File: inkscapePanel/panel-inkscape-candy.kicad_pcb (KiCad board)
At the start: 2 copper layers, 99.9 x 38.9 mm, 39 parts

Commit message: new panel
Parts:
- removed the G*** at (0.00, 0.00) (x6)
- added G*** (x6): LOGO, LOGO, F.Cu at (0.00, 0.00)

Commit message: single
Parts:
- removed the G*** at (0.00, 0.00) (x6)
- added G*** (x6): LOGO, LOGO, F.Cu at (0.00, 0.00)

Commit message: sent to fab
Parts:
- removed the ? at (47.0, 28.6)
- removed the ? at (30.8, 34.3)
- removed the ? at (14.2, 28.6)
- removed the ? at (14.3, 29.6)
- removed the ? at (14.3, 30.5)
- removed the ? at (14.2, 31.4)
- removed the ? at (16.6, 28.7)
- removed the ? at (16.6, 29.6)
- removed the ? at (47.0, 29.6)
- removed the ? at (16.6, 30.5)
- removed the ? at (16.6, 31.4)
- removed the ? at (47.0, 30.5)
- removed the ? at (-46.7, 28.7)
- removed the ? at (-46.8, 29.7)
- removed the ? at (-46.8, 30.6)
- removed the ? at (-46.7, 31.5)
- removed the ? at (47.0, 31.4)
- removed the ? at (19.0, 28.6)
- removed the G*** at (0.00, 0.00) (x6)
- added ?: , Wire_Pads:SolderWirePad_single_0-8mmDrill, F.Cu at (44.8, 28.9)
- added ?: , Wire_Pads:SolderWirePad_single_0-8mmDrill, F.Cu at (30.7, 34.0)
- added ?: , Wire_Pads:SolderWirePad_single_0-8mmDrill, F.Cu at (14.3, 28.7)
- added ?: , Wire_Pads:SolderWirePad_single_0-8mmDrill, F.Cu at (14.4, 29.7)
- added ?: , Wire_Pads:SolderWirePad_single_0-8mmDrill, F.Cu at (14.4, 30.6)
- added ?: , Wire_Pads:SolderWirePad_single_0-8mmDrill, F.Cu at (14.4, 31.4)
- added ?: , Wire_Pads:SolderWirePad_single_0-8mmDrill, F.Cu at (16.5, 28.8)
- added ?: , Wire_Pads:SolderWirePad_single_0-8mmDrill, F.Cu at (16.4, 29.6)
- added ?: , Wire_Pads:SolderWirePad_single_0-8mmDrill, F.Cu at (45.0, 29.7)
- added ?: , Wire_Pads:SolderWirePad_single_0-8mmDrill, F.Cu at (16.4, 30.6)
- added ?: , Wire_Pads:SolderWirePad_single_0-8mmDrill, F.Cu at (16.5, 31.3)
- added ?: , Wire_Pads:SolderWirePad_single_0-8mmDrill, F.Cu at (45.0, 30.5)
- added ?: , Wire_Pads:SolderWirePad_single_0-8mmDrill, F.Cu at (-44.6, 28.8)
- added ?: , Wire_Pads:SolderWirePad_single_0-8mmDrill, F.Cu at (-44.7, 29.7)
- added ?: , Wire_Pads:SolderWirePad_single_0-8mmDrill, F.Cu at (-44.7, 30.6)
- added ?: , Wire_Pads:SolderWirePad_single_0-8mmDrill, F.Cu at (-44.7, 31.4)
- added ?: , Wire_Pads:SolderWirePad_single_0-8mmDrill, F.Cu at (44.9, 31.4)
- added ?: , Wire_Pads:SolderWirePad_single_0-8mmDrill, F.Cu at (19.0, 28.5)
- added G*** (x6): LOGO, LOGO, F.Cu at (0.00, 0.00)

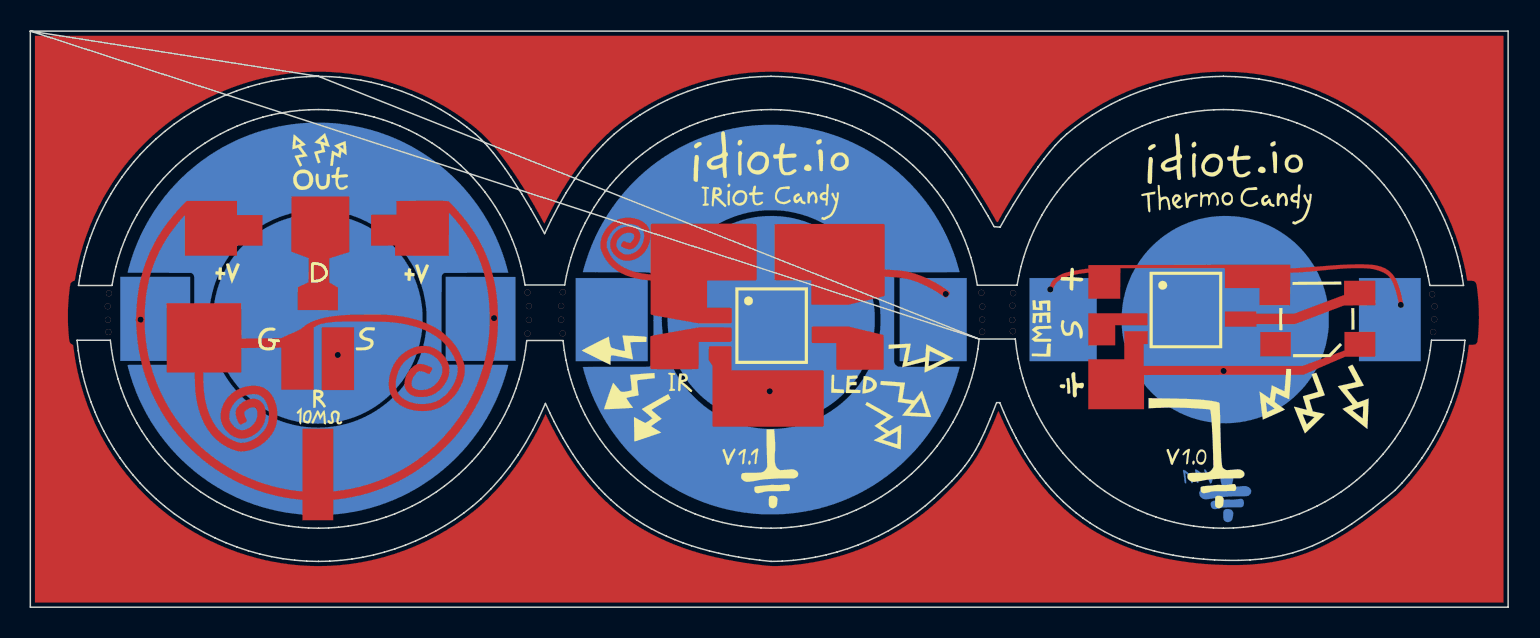
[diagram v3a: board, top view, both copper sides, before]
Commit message: thinner outlines, more back ground space
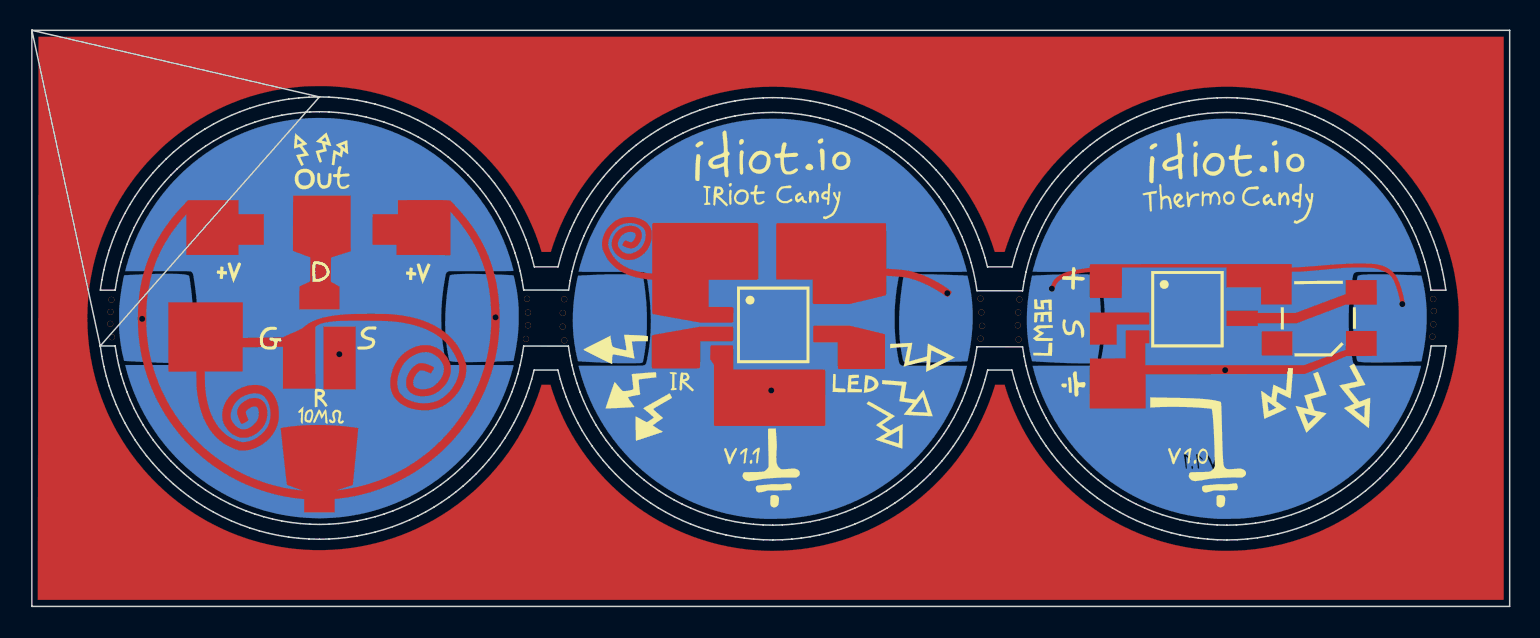
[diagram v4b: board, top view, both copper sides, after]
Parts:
- removed the ? at (44.8, 28.9)
- removed the ? at (30.7, 34.0)
- removed the ? at (-18.6, 30.5)
- removed the ? at (-29.2, 33.0)
- removed the ? at (-42.5, 30.6)
- removed the ? at (14.3, 28.7)
- removed the ? at (14.4, 29.7)
- removed the ? at (14.4, 30.6)
- removed the ? at (14.4, 31.4)
- removed the ? at (16.5, 28.8)
- removed the ? at (16.4, 29.6)
- removed the ? at (45.0, 29.7)
- removed the ? at (16.4, 30.6)
- removed the ? at (16.5, 31.3)
- removed the ? at (-16.3, 28.7)
- removed the ? at (-16.2, 29.7)
- removed the ? at (-16.2, 30.6)
- removed the ? at (-16.3, 31.5)
- removed the ? at (-14.0, 28.7)
- removed the ? at (-14.1, 29.6)
- removed the ? at (-14.1, 30.6)
- removed the ? at (-14.0, 31.5)
- removed the ? at (45.0, 30.5)
- removed the ? at (-44.6, 28.8)
- removed the ? at (-44.7, 29.7)
- removed the ? at (-44.7, 30.6)
- removed the ? at (-44.7, 31.4)
- removed the ? at (44.9, 31.4)
- removed the ? at (11.9, 28.8)
- removed the ? at (0.03, 35.4)
- removed the ? at (42.7, 29.6)
- removed the ? at (19.0, 28.5)
- removed the G*** at (0.00, 0.00) (x6)
- added ?: , Wire_Pads:SolderWirePad_single_0-8mmDrill, F.Cu at (44.9, 29.2)
- added ?: , Wire_Pads:SolderWirePad_single_0-8mmDrill, F.Cu at (30.8, 34.0)
- added ?: , Wire_Pads:SolderWirePad_single_0-8mmDrill, F.Cu at (-18.5, 30.4)
- added ?: , Wire_Pads:SolderWirePad_single_0-8mmDrill, F.Cu at (-29.1, 32.9)
- added ?: , Wire_Pads:SolderWirePad_single_0-8mmDrill, F.Cu at (-42.4, 30.5)
- added ?: , Wire_Pads:SolderWirePad_single_0-8mmDrill, F.Cu at (14.3, 29.1)
- added ?: , Wire_Pads:SolderWirePad_single_0-8mmDrill, F.Cu at (14.3, 30.1)
- added ?: , Wire_Pads:SolderWirePad_single_0-8mmDrill, F.Cu at (14.4, 31.0)
- added ?: , Wire_Pads:SolderWirePad_single_0-8mmDrill, F.Cu at (14.3, 31.8)
- added ?: , Wire_Pads:SolderWirePad_single_0-8mmDrill, F.Cu at (16.9, 29.2)
- added ?: , Wire_Pads:SolderWirePad_single_0-8mmDrill, F.Cu at (16.8, 30.1)
- added ?: , Wire_Pads:SolderWirePad_single_0-8mmDrill, F.Cu at (44.9, 30.0)
- added ?: , Wire_Pads:SolderWirePad_single_0-8mmDrill, F.Cu at (16.8, 30.9)
- added ?: , Wire_Pads:SolderWirePad_single_0-8mmDrill, F.Cu at (16.9, 31.9)
- added ?: , Wire_Pads:SolderWirePad_single_0-8mmDrill, F.Cu at (-16.4, 29.2)
- added ?: , Wire_Pads:SolderWirePad_single_0-8mmDrill, F.Cu at (-16.3, 30.1)
- added ?: , Wire_Pads:SolderWirePad_single_0-8mmDrill, F.Cu at (-16.3, 31.0)
- added ?: , Wire_Pads:SolderWirePad_single_0-8mmDrill, F.Cu at (-16.4, 31.9)
- added ?: , Wire_Pads:SolderWirePad_single_0-8mmDrill, F.Cu at (-13.9, 29.2)
- added ?: , Wire_Pads:SolderWirePad_single_0-8mmDrill, F.Cu at (-14.0, 30.1)
- added ?: , Wire_Pads:SolderWirePad_single_0-8mmDrill, F.Cu at (-14.0, 31.0)
- added ?: , Wire_Pads:SolderWirePad_single_0-8mmDrill, F.Cu at (-13.9, 32.0)
- added ?: , Wire_Pads:SolderWirePad_single_0-8mmDrill, F.Cu at (44.9, 30.9)
- added ?: , Wire_Pads:SolderWirePad_single_0-8mmDrill, F.Cu at (-44.5, 29.2)
- added ?: , Wire_Pads:SolderWirePad_single_0-8mmDrill, F.Cu at (-44.5, 30.0)
- added ?: , Wire_Pads:SolderWirePad_single_0-8mmDrill, F.Cu at (-44.5, 30.8)
- added ?: , Wire_Pads:SolderWirePad_single_0-8mmDrill, F.Cu at (-44.4, 31.7)
- added ?: , Wire_Pads:SolderWirePad_single_0-8mmDrill, F.Cu at (44.8, 31.7)
- added ?: , Wire_Pads:SolderWirePad_single_0-8mmDrill, F.Cu at (12.0, 28.8)
- added ?: , Wire_Pads:SolderWirePad_single_0-8mmDrill, F.Cu at (0.14, 35.3)
- added ?: , Wire_Pads:SolderWirePad_single_0-8mmDrill, F.Cu at (42.8, 29.5)
- added ?: , Wire_Pads:SolderWirePad_single_0-8mmDrill, F.Cu at (19.1, 28.5)
- added G*** (x6): LOGO, LOGO, F.Cu at (0.00, 0.00)
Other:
- outline, holes or cut-outs redrawn
